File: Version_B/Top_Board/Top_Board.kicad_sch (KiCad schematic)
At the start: 3 parts, among them J1 90_Deg_Conn, J2 90_Deg_Conn, U1 T-Display-S3

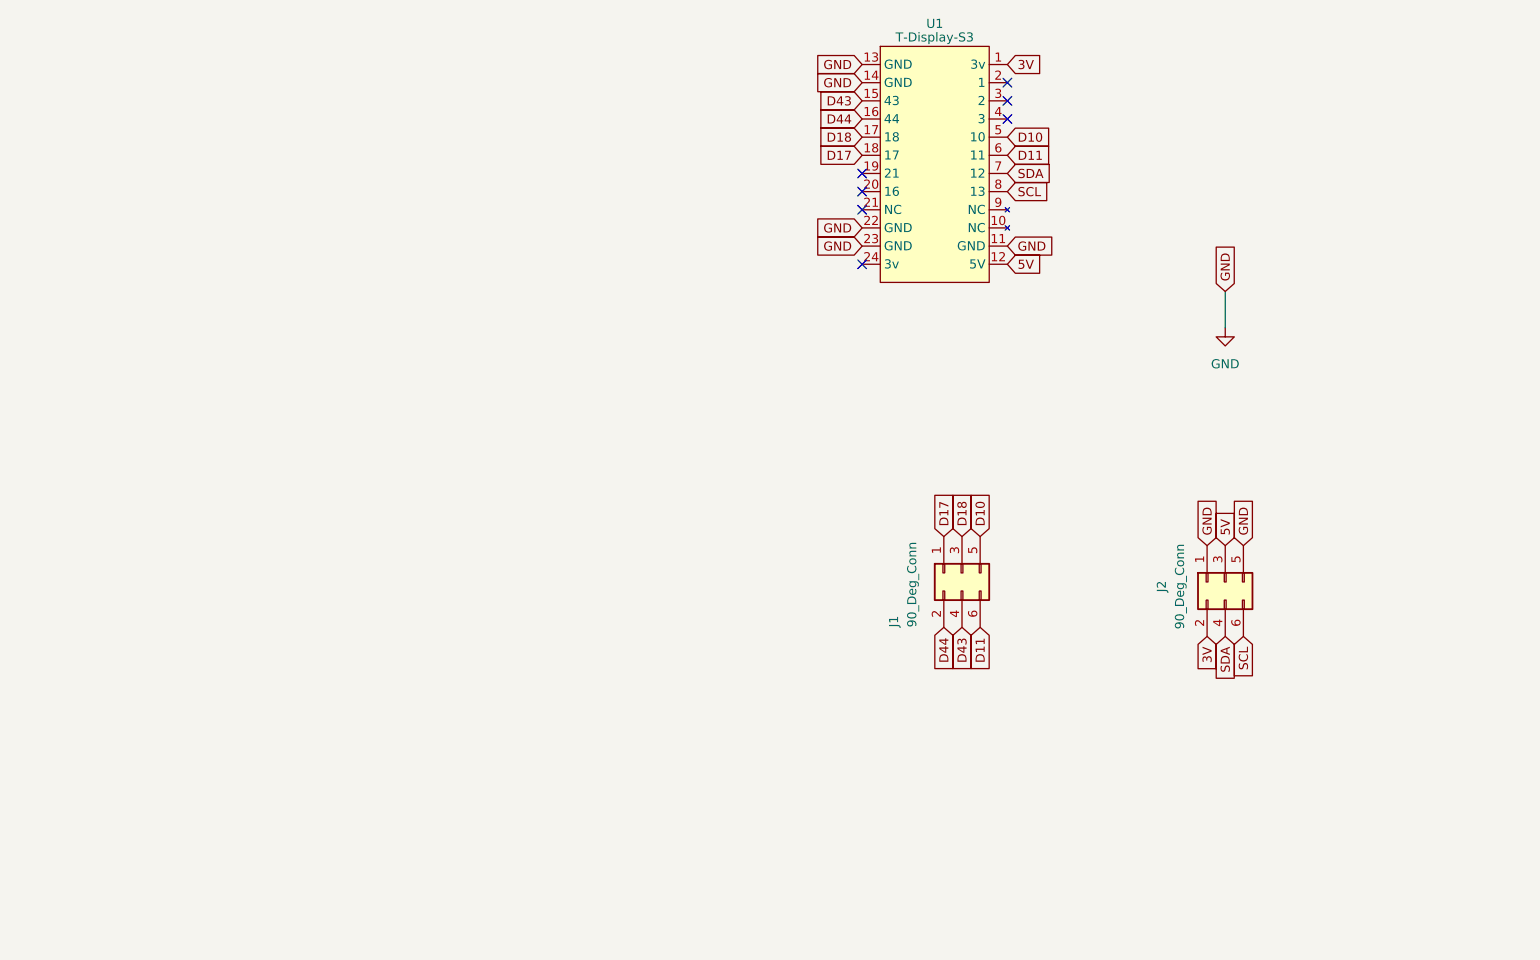
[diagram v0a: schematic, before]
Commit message: fixed directory overwrite
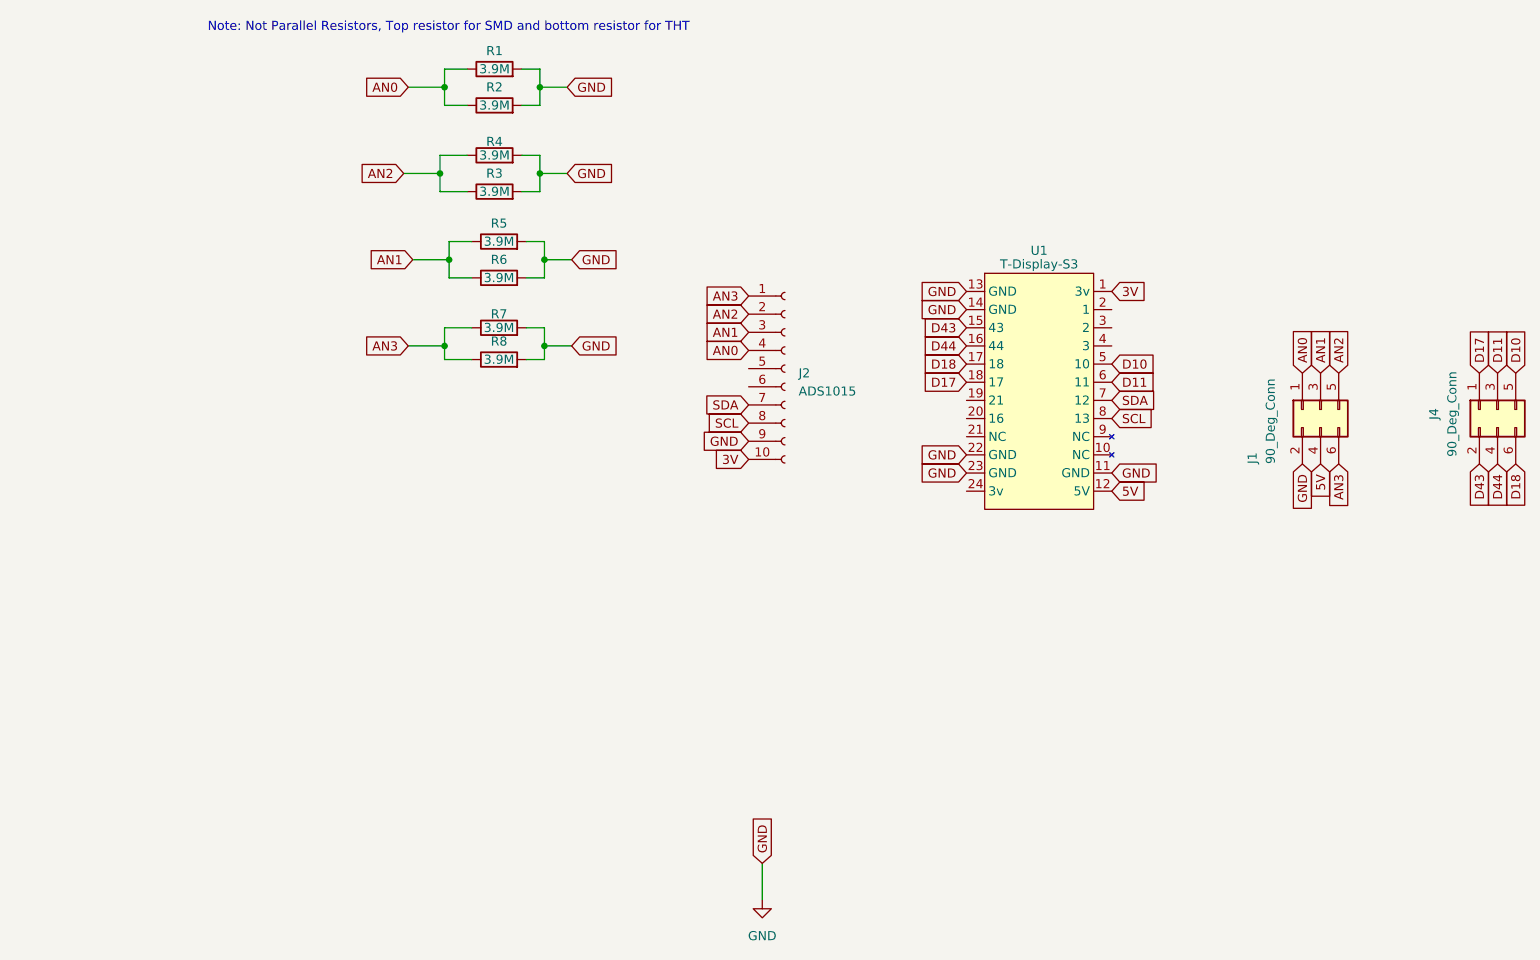
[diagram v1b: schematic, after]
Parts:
- added J2: ADS1015, Voltage_Sensor_Timer:PinSocket_1x10_P2.54mm_Vertical_1, symbol Connector:Conn_01x10_Socket
- added R1, R4, R5, R7: 3.9M, Resistor_SMD:R_0805_2012Metric, symbol Device:R
- added R2, R3, R6, R8: 3.9M, Resistor_THT:R_Axial_DIN0411_L9.9mm_D3.6mm_P12.70mm_Horizontal, symbol Device:R
- renumbered J2 to J4
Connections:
- net 3V: now also J2.10 (Pin_10); no longer J4.2 (Pin_2)
- net 5V: now also J1.4 (Pin_4); no longer J4.3 (Pin_3)
- net D10: now also J4.5 (Pin_5); no longer J1.5 (Pin_5)
- net D11: now also J4.3 (Pin_3); no longer J1.6 (Pin_6)
- net D17: now also J4.1 (Pin_1); no longer J1.1 (Pin_1)
- net D18: now also J4.6 (Pin_6); no longer J1.3 (Pin_3)
- net D43: now also J4.2 (Pin_2); no longer J1.4 (Pin_4)
- net D44: now also J4.4 (Pin_4); no longer J1.2 (Pin_2)
- net GND: now also J1.2 (Pin_2), J2.9 (Pin_9), R1.2, R2.2, R3.2, R4.2, R5.2, R6.2, R7.2, R8.2; no longer J4.1 (Pin_1), J4.5 (Pin_5)
- net SCL: now also J2.8 (Pin_8); no longer J4.6 (Pin_6)
- net SDA: now also J2.7 (Pin_7); no longer J4.4 (Pin_4)
- new net AN0: J1.1 (Pin_1), J2.4 (Pin_4), R1.1, R2.1
- new net AN1: J1.3 (Pin_3), J2.3 (Pin_3), R5.1, R6.1
- new net AN2: J1.5 (Pin_5), J2.2 (Pin_2), R3.1, R4.1
- new net AN3: J1.6 (Pin_6), J2.1 (Pin_1), R7.1, R8.1
- no-connect marks 7 -> 0
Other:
- note added: "Note: Not Parallel Resistors, Top resistor for SMD and bottom resistor for THT"
- company: Secured Solutions Group -> (none)
- title: Current Monitoring System (Top Board) -> Top_Board
- moved on the sheet: J1, J4, U1

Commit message: ads1015 on bottom board and aesthetic changes
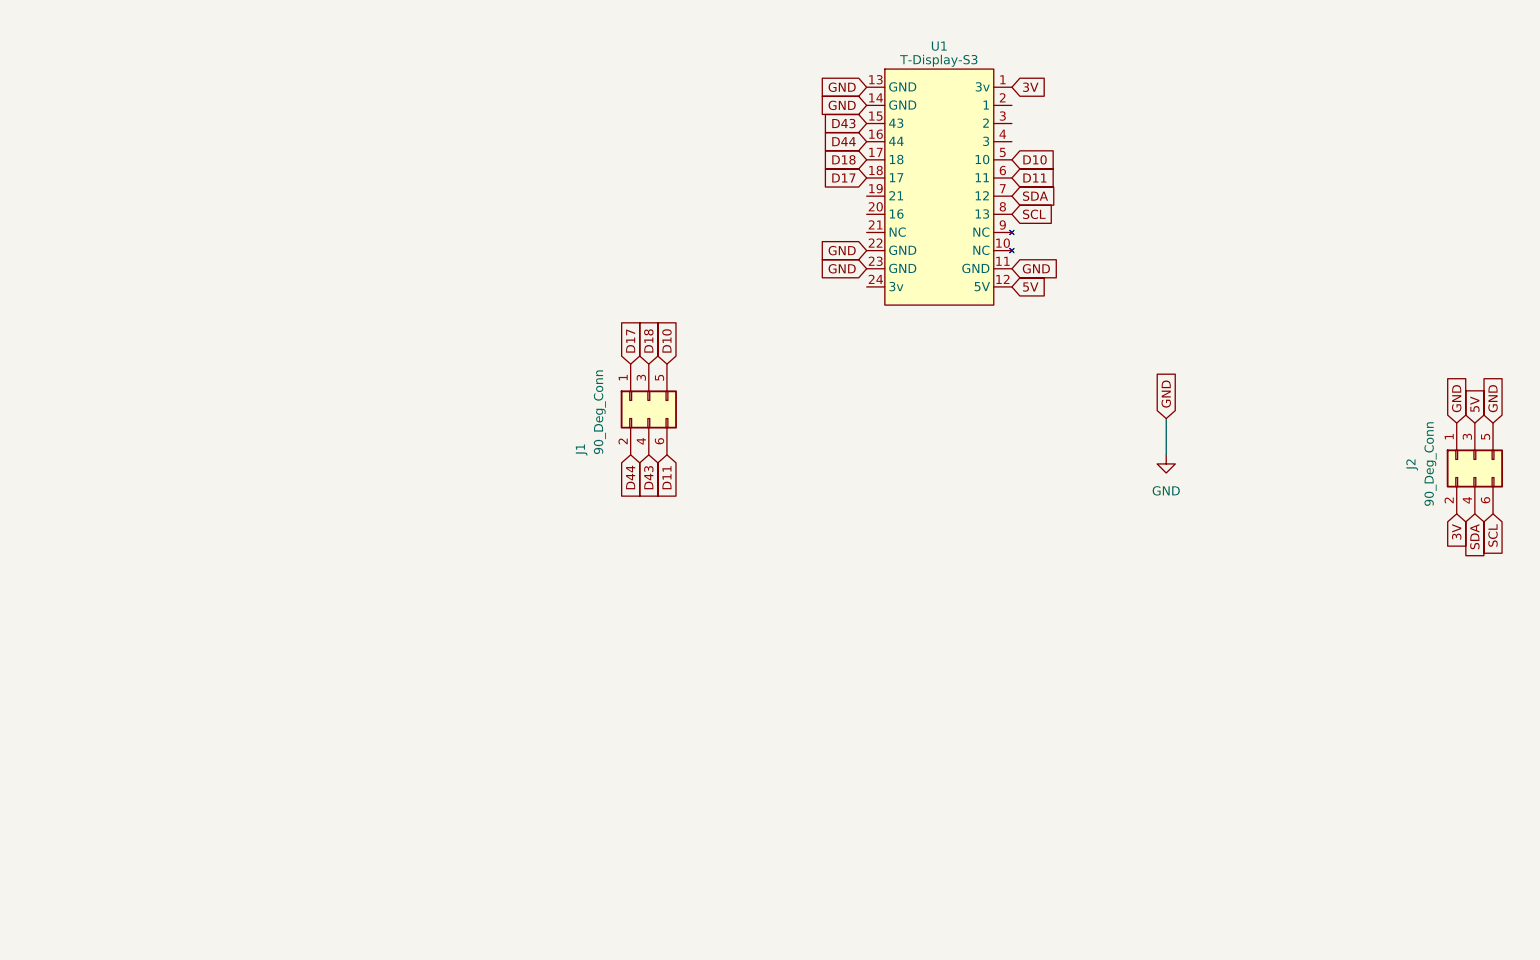
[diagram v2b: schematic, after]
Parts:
- removed J2: ADS1015, Voltage_Sensor_Timer:PinSocket_1x10_P2.54mm_Vertical_1, symbol Connector:Conn_01x10_Socket
- removed R1, R4, R5, R7: 3.9M, Resistor_SMD:R_0805_2012Metric, symbol Device:R
- removed R2, R3, R6, R8: 3.9M, Resistor_THT:R_Axial_DIN0411_L9.9mm_D3.6mm_P12.70mm_Horizontal, symbol Device:R
- renumbered J4 to J2
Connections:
- net AN0 is gone; now on net D17: J1.1 (Pin_1)
- net AN1 is gone; now on net D18: J1.3 (Pin_3)
- net AN2 is gone; now on net D10: J1.5 (Pin_5)
- net AN3 is gone; now on net D11: J1.6 (Pin_6)
- net 3V: now also J2.2 (Pin_2)
- net 5V: now also J2.3 (Pin_3); no longer J1.4 (Pin_4)
- net D10: no longer J2.5 (Pin_5)
- net D11: no longer J2.3 (Pin_3)
- net D17: no longer J2.1 (Pin_1)
- net D18: no longer J2.6 (Pin_6)
- net D43: now also J1.4 (Pin_4); no longer J2.2 (Pin_2)
- net D44: now also J1.2 (Pin_2); no longer J2.4 (Pin_4)
- net GND: now also J2.1 (Pin_1), J2.5 (Pin_5); no longer J1.2 (Pin_2)
- net SCL: now also J2.6 (Pin_6)
- net SDA: now also J2.4 (Pin_4)
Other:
- note removed: "Note: Not Parallel Resistors, Top resistor for SMD and bottom resistor for THT"
- moved on the sheet: J1, J2, U1

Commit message: added flash folder and adjusted GUI
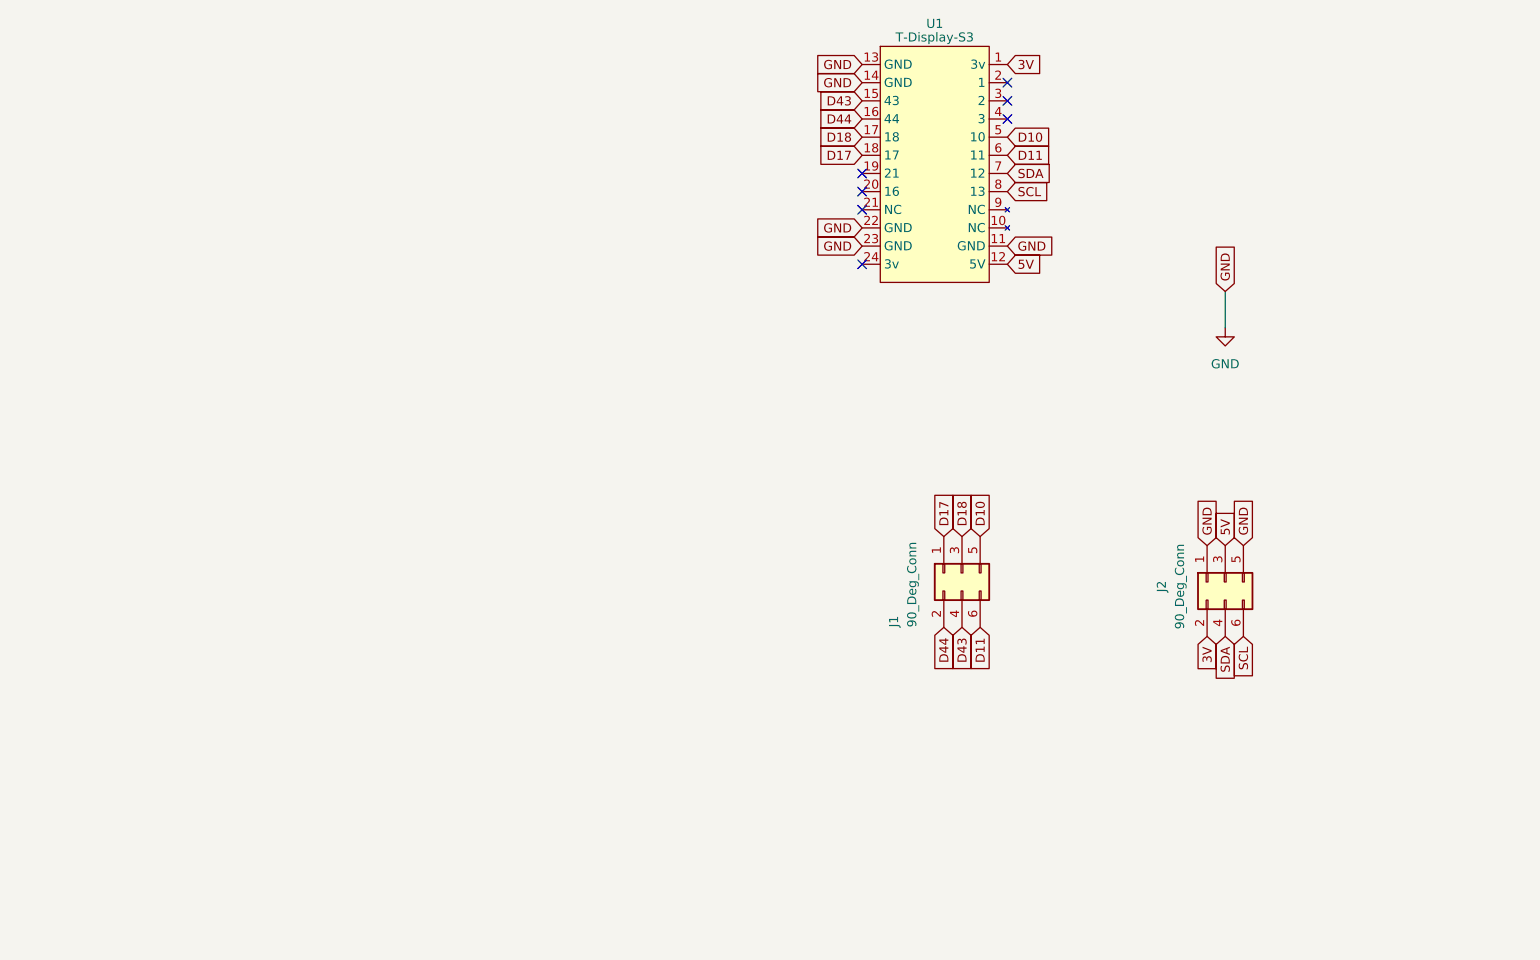
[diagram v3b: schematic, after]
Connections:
- no-connect marks 0 -> 7
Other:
- company: (none) -> Secured Solutions Group
- title: Top_Board -> Current Monitoring System (Top Board)
- moved on the sheet: J1, J2, U1
